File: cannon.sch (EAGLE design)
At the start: 55 parts, among them J1 RJ45

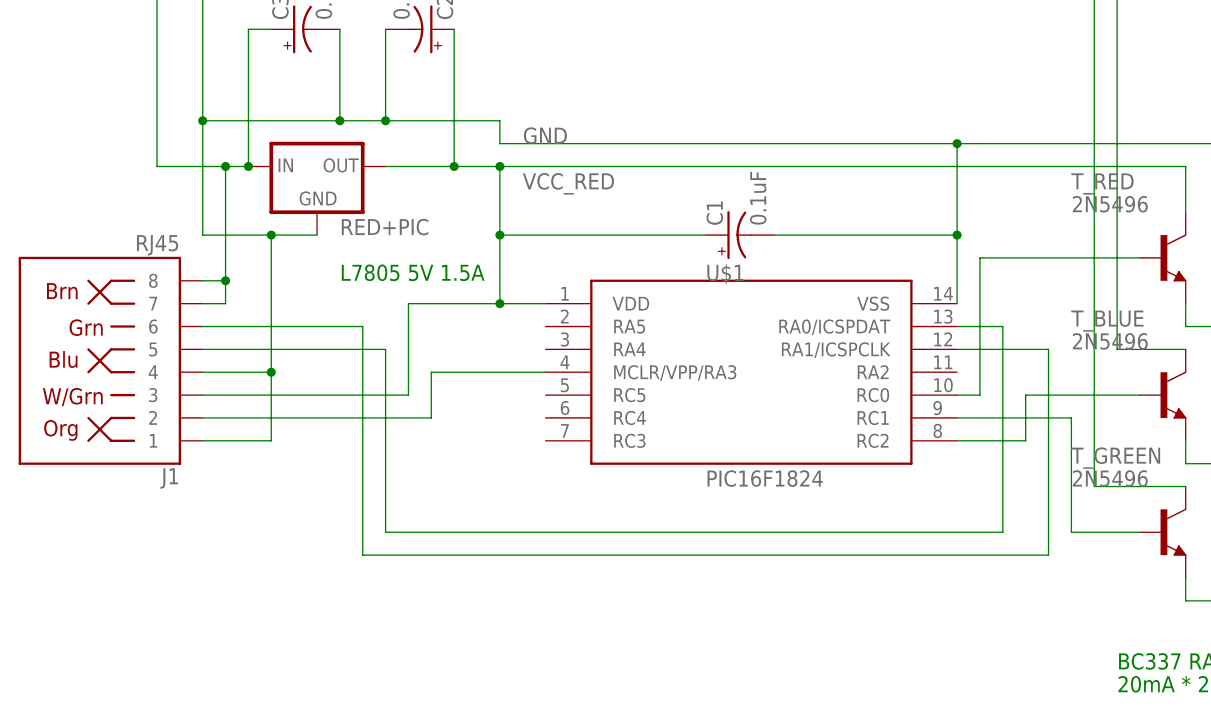
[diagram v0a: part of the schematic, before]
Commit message: Updated Board, Removed In Circuit programming
Adjusted RJ45 pins for POE standard BOARD DESIGN NOT CHANGED!!! DO NOT USE TO MAKE BOARDS
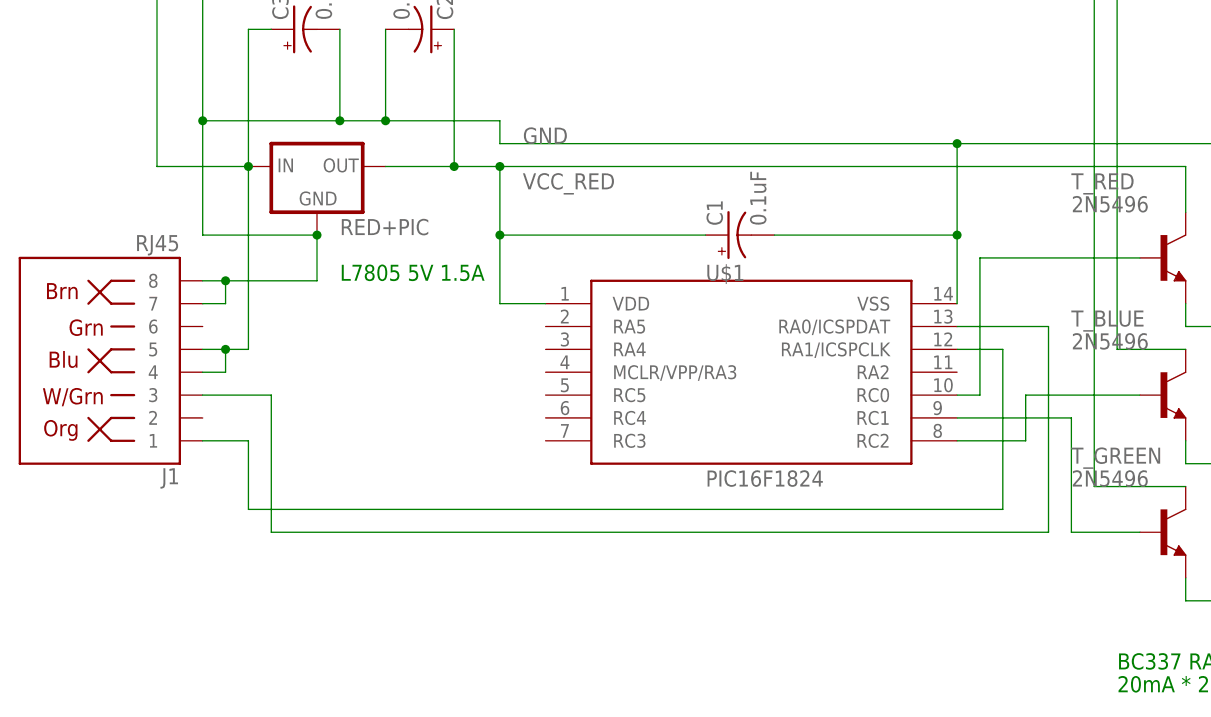
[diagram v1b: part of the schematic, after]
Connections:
- removed net N$23: J1.5, U$1.RA0/ICSPDAT
- removed net N$24: J1.6, U$1.RA1/ICSPCLK
- removed net N$8: J1.2, U$1.MCLR/VPP/RA3
- new net N$1: J1.1, U$1.RA1/ICSPCLK
- new net N$2: J1.3, U$1.RA0/ICSPDAT
- net GND: now also J1.7, J1.8; no longer J1.1, J1.4
- net N$25: now also J1.4, J1.5; no longer J1.7, J1.8
- net VCC_RED: no longer J1.3
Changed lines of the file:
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@@
 <?xml version="1.0" encoding="utf-8"?>
 <!DOCTYPE eagle SYSTEM "eagle.dtd">
-<eagle version="9.3.0">
+<eagle version="9.3.2">
 <drawing>
 <settings>
@@
 <wire x1="-12.7" y1="71.12" x2="10.16" y2="71.12" width="0.1524" layer="91"/>
 <junction x="-12.7" y="71.12"/>
-<pinref part="J1" gate="JP1" pin="3"/>
-<wire x1="-45.72" y1="53.34" x2="-22.86" y2="53.34" width="0.1524" layer="91"/>
-<wire x1="-22.86" y1="53.34" x2="-22.86" y2="63.5" width="0.1524" layer="91"/>
-<wire x1="-22.86" y1="63.5" x2="-12.7" y2="63.5" width="0.1524" layer="91"/>
-<junction x="-12.7" y="63.5"/>
 <pinref part="C2" gate="G$1" pin="+"/>
 <wire x1="-17.78" y1="93.98" x2="-17.78" y2="78.74" width="0.1524" layer="91"/>
@@
 </segment>
 </net>
-<net name="N$23" class="0">
-<segment>
-<pinref part="U$1" gate="G$1" pin="RA0/ICSPDAT"/>
-<wire x1="38.1" y1="60.96" x2="43.18" y2="60.96" width="0.1524" layer="91"/>
-<wire x1="43.18" y1="60.96" x2="43.18" y2="38.1" width="0.1524" layer="91"/>
-<pinref part="J1" gate="JP1" pin="5"/>
-<wire x1="-45.72" y1="58.42" x2="-25.4" y2="58.42" width="0.1524" layer="91"/>
-<wire x1="-25.4" y1="58.42" x2="-25.4" y2="38.1" width="0.1524" layer="91"/>
-<wire x1="-25.4" y1="38.1" x2="43.18" y2="38.1" width="0.1524" layer="91"/>
-</segment>
-</net>
-<net name="N$24" class="0">
-<segment>
-<pinref part="U$1" gate="G$1" pin="RA1/ICSPCLK"/>
-<wire x1="38.1" y1="58.42" x2="48.26" y2="58.42" width="0.1524" layer="91"/>
-<wire x1="48.26" y1="58.42" x2="48.26" y2="35.56" width="0.1524" layer="91"/>
-<pinref part="J1" gate="JP1" pin="6"/>
-<wire x1="-45.72" y1="60.96" x2="-27.94" y2="60.96" width="0.1524" layer="91"/>
-<wire x1="-27.94" y1="60.96" x2="-27.94" y2="35.56" width="0.1524" layer="91"/>
-<wire x1="-27.94" y1="35.56" x2="48.26" y2="35.56" width="0.1524" layer="91"/>
-</segment>
-</net>
-<net name="N$8" class="0">
-<segment>
-<pinref part="J1" gate="JP1" pin="2"/>
-<wire x1="-45.72" y1="50.8" x2="-20.32" y2="50.8" width="0.1524" layer="91"/>
-<wire x1="-20.32" y1="50.8" x2="-20.32" y2="55.88" width="0.1524" layer="91"/>
-<pinref part="U$1" gate="G$1" pin="MCLR/VPP/RA3"/>
-<wire x1="-20.32" y1="55.88" x2="-7.62" y2="55.88" width="0.1524" layer="91"/>
-</segment>
-</net>
 <net name="VCC_BLUE" class="0">
 <segment>
@@
 <wire x1="-40.64" y1="121.92" x2="-50.8" y2="121.92" width="0.1524" layer="91"/>
 <junction x="-40.64" y="121.92"/>
-<wire x1="-43.18" y1="78.74" x2="-40.64" y2="78.74" width="0.1524" layer="91"/>
-<pinref part="J1" gate="JP1" pin="8"/>
-<wire x1="-45.72" y1="66.04" x2="-43.18" y2="66.04" width="0.1524" layer="91"/>
-<wire x1="-43.18" y1="66.04" x2="-43.18" y2="78.74" width="0.1524" layer="91"/>
-<pinref part="J1" gate="JP1" pin="7"/>
-<wire x1="-45.72" y1="63.5" x2="-43.18" y2="63.5" width="0.1524" layer="91"/>
-<wire x1="-43.18" y1="63.5" x2="-43.18" y2="66.04" width="0.1524" layer="91"/>
-<junction x="-43.18" y="66.04"/>
 <pinref part="C3" gate="G$1" pin="+"/>
 <wire x1="-38.1" y1="93.98" x2="-40.64" y2="93.98" width="0.1524" layer="91"/>
@@
 <junction x="-40.64" y="78.74"/>
 <wire x1="-50.8" y1="121.92" x2="-50.8" y2="78.74" width="0.1524" layer="91"/>
-<wire x1="-50.8" y1="78.74" x2="-43.18" y2="78.74" width="0.1524" layer="91"/>
-<junction x="-43.18" y="78.74"/>
+<wire x1="-50.8" y1="78.74" x2="-40.64" y2="78.74" width="0.1524" layer="91"/>
 <pinref part="BLUE" gate="G$1" pin="IN"/>
 <wire x1="-40.64" y1="154.94" x2="-50.8" y2="154.94" width="0.1524" layer="91"/>
@@
 <wire x1="-40.64" y1="170.18" x2="-40.64" y2="154.94" width="0.1524" layer="91"/>
 <junction x="-40.64" y="154.94"/>
+<pinref part="J1" gate="JP1" pin="5"/>
+<wire x1="-40.64" y1="58.42" x2="-40.64" y2="78.74" width="0.1524" layer="91"/>
+<wire x1="-45.72" y1="58.42" x2="-43.18" y2="58.42" width="0.1524" layer="91"/>
+<pinref part="J1" gate="JP1" pin="4"/>
+<wire x1="-43.18" y1="58.42" x2="-40.64" y2="58.42" width="0.1524" layer="91"/>
+<wire x1="-45.72" y1="55.88" x2="-43.18" y2="55.88" width="0.1524" layer="91"/>
+<wire x1="-43.18" y1="55.88" x2="-43.18" y2="58.42" width="0.1524" layer="91"/>
+<junction x="-43.18" y="58.42"/>
 </segment>
 </net>
@@
 <wire x1="38.1" y1="81.28" x2="-12.7" y2="81.28" width="0.1524" layer="91"/>
 <junction x="38.1" y="81.28"/>
-<wire x1="-33.02" y1="71.12" x2="-38.1" y2="71.12" width="0.1524" layer="91"/>
-<wire x1="-38.1" y1="71.12" x2="-45.72" y2="71.12" width="0.1524" layer="91"/>
+<wire x1="-33.02" y1="71.12" x2="-45.72" y2="71.12" width="0.1524" layer="91"/>
 <wire x1="-45.72" y1="71.12" x2="-45.72" y2="83.82" width="0.1524" layer="91"/>
 <wire x1="-45.72" y1="83.82" x2="-30.48" y2="83.82" width="0.1524" layer="91"/>
@@
 <wire x1="17.78" y1="71.12" x2="38.1" y2="71.12" width="0.1524" layer="91"/>
 <junction x="38.1" y="71.12"/>
-<pinref part="J1" gate="JP1" pin="1"/>
-<wire x1="-45.72" y1="48.26" x2="-38.1" y2="48.26" width="0.1524" layer="91"/>
-<wire x1="-38.1" y1="48.26" x2="-38.1" y2="55.88" width="0.1524" layer="91"/>
-<junction x="-38.1" y="71.12"/>
-<pinref part="J1" gate="JP1" pin="4"/>
-<wire x1="-38.1" y1="55.88" x2="-38.1" y2="71.12" width="0.1524" layer="91"/>
-<wire x1="-45.72" y1="55.88" x2="-38.1" y2="55.88" width="0.1524" layer="91"/>
-<junction x="-38.1" y="55.88"/>
 <pinref part="C3" gate="G$1" pin="-"/>
 <wire x1="-30.48" y1="93.98" x2="-30.48" y2="83.82" width="0.1524" layer="91"/>
@@
 <junction x="254" y="66.04"/>
 <wire x1="254" y1="66.04" x2="292.1" y2="66.04" width="0.1524" layer="91"/>
+<pinref part="J1" gate="JP1" pin="8"/>
+<wire x1="-45.72" y1="66.04" x2="-43.18" y2="66.04" width="0.1524" layer="91"/>
+<wire x1="-43.18" y1="66.04" x2="-33.02" y2="66.04" width="0.1524" layer="91"/>
+<wire x1="-33.02" y1="66.04" x2="-33.02" y2="71.12" width="0.1524" layer="91"/>
+<junction x="-33.02" y="71.12"/>
+<pinref part="J1" gate="JP1" pin="7"/>
+<wire x1="-45.72" y1="63.5" x2="-43.18" y2="63.5" width="0.1524" layer="91"/>
+<wire x1="-43.18" y1="63.5" x2="-43.18" y2="66.04" width="0.1524" layer="91"/>
+<junction x="-43.18" y="66.04"/>
 </segment>
 </net>
@@
 </segment>
 </net>
+<net name="N$1" class="0">
+<segment>
+<pinref part="U$1" gate="G$1" pin="RA1/ICSPCLK"/>
+<wire x1="38.1" y1="58.42" x2="43.18" y2="58.42" width="0.1524" layer="91"/>
+<wire x1="43.18" y1="58.42" x2="43.18" y2="40.64" width="0.1524" layer="91"/>
+<wire x1="43.18" y1="40.64" x2="-40.64" y2="40.64" width="0.1524" layer="91"/>
+<wire x1="-40.64" y1="40.64" x2="-40.64" y2="48.26" width="0.1524" layer="91"/>
+<pinref part="J1" gate="JP1" pin="1"/>
+<wire x1="-40.64" y1="48.26" x2="-45.72" y2="48.26" width="0.1524" layer="91"/>
+</segment>
+</net>
+<net name="N$2" class="0">
+<segment>
+<pinref part="U$1" gate="G$1" pin="RA0/ICSPDAT"/>
+<wire x1="38.1" y1="60.96" x2="48.26" y2="60.96" width="0.1524" layer="91"/>
+<wire x1="48.26" y1="60.96" x2="48.26" y2="38.1" width="0.1524" layer="91"/>
+<wire x1="48.26" y1="38.1" x2="-38.1" y2="38.1" width="0.1524" layer="91"/>
+<pinref part="J1" gate="JP1" pin="3"/>
+<wire x1="-38.1" y1="38.1" x2="-38.1" y2="53.34" width="0.1524" layer="91"/>
+<wire x1="-38.1" y1="53.34" x2="-45.72" y2="53.34" width="0.1524" layer="91"/>
+</segment>
+</net>

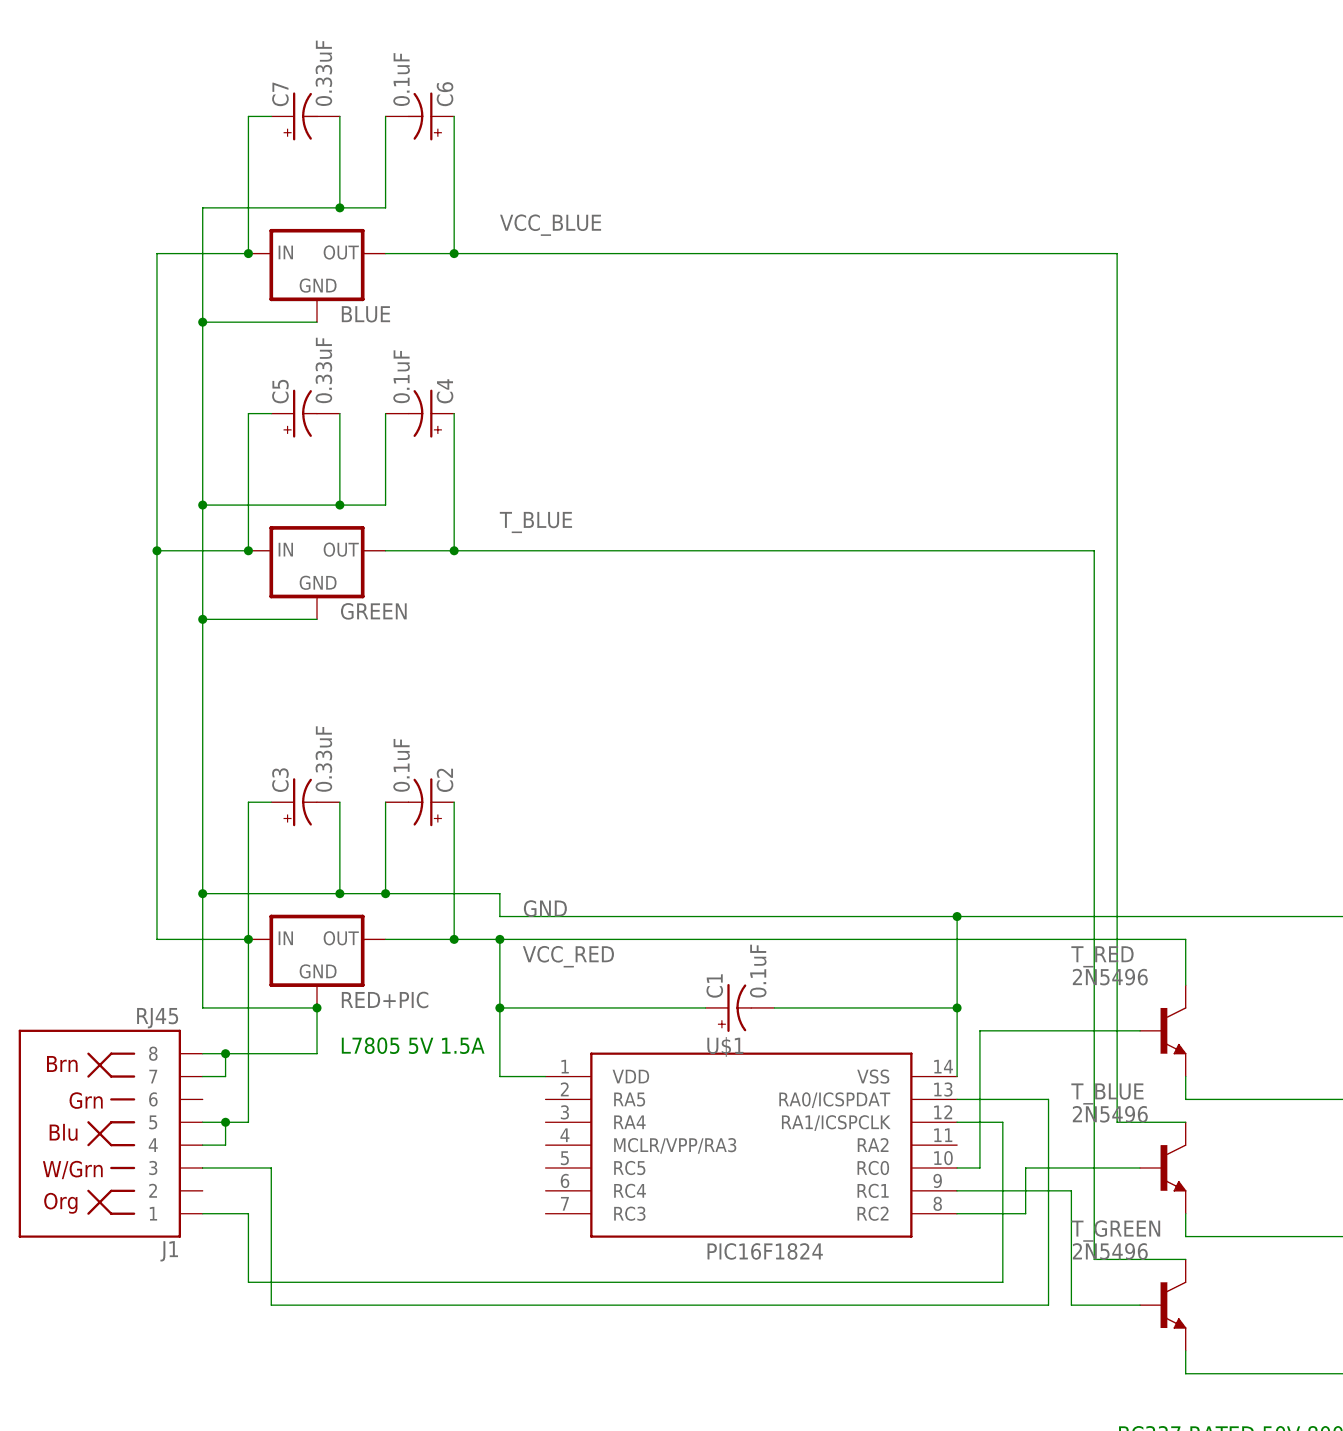
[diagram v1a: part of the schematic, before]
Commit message: Updated everything
Updated capacitor size, transistor pad, power reg pad, and LED pad
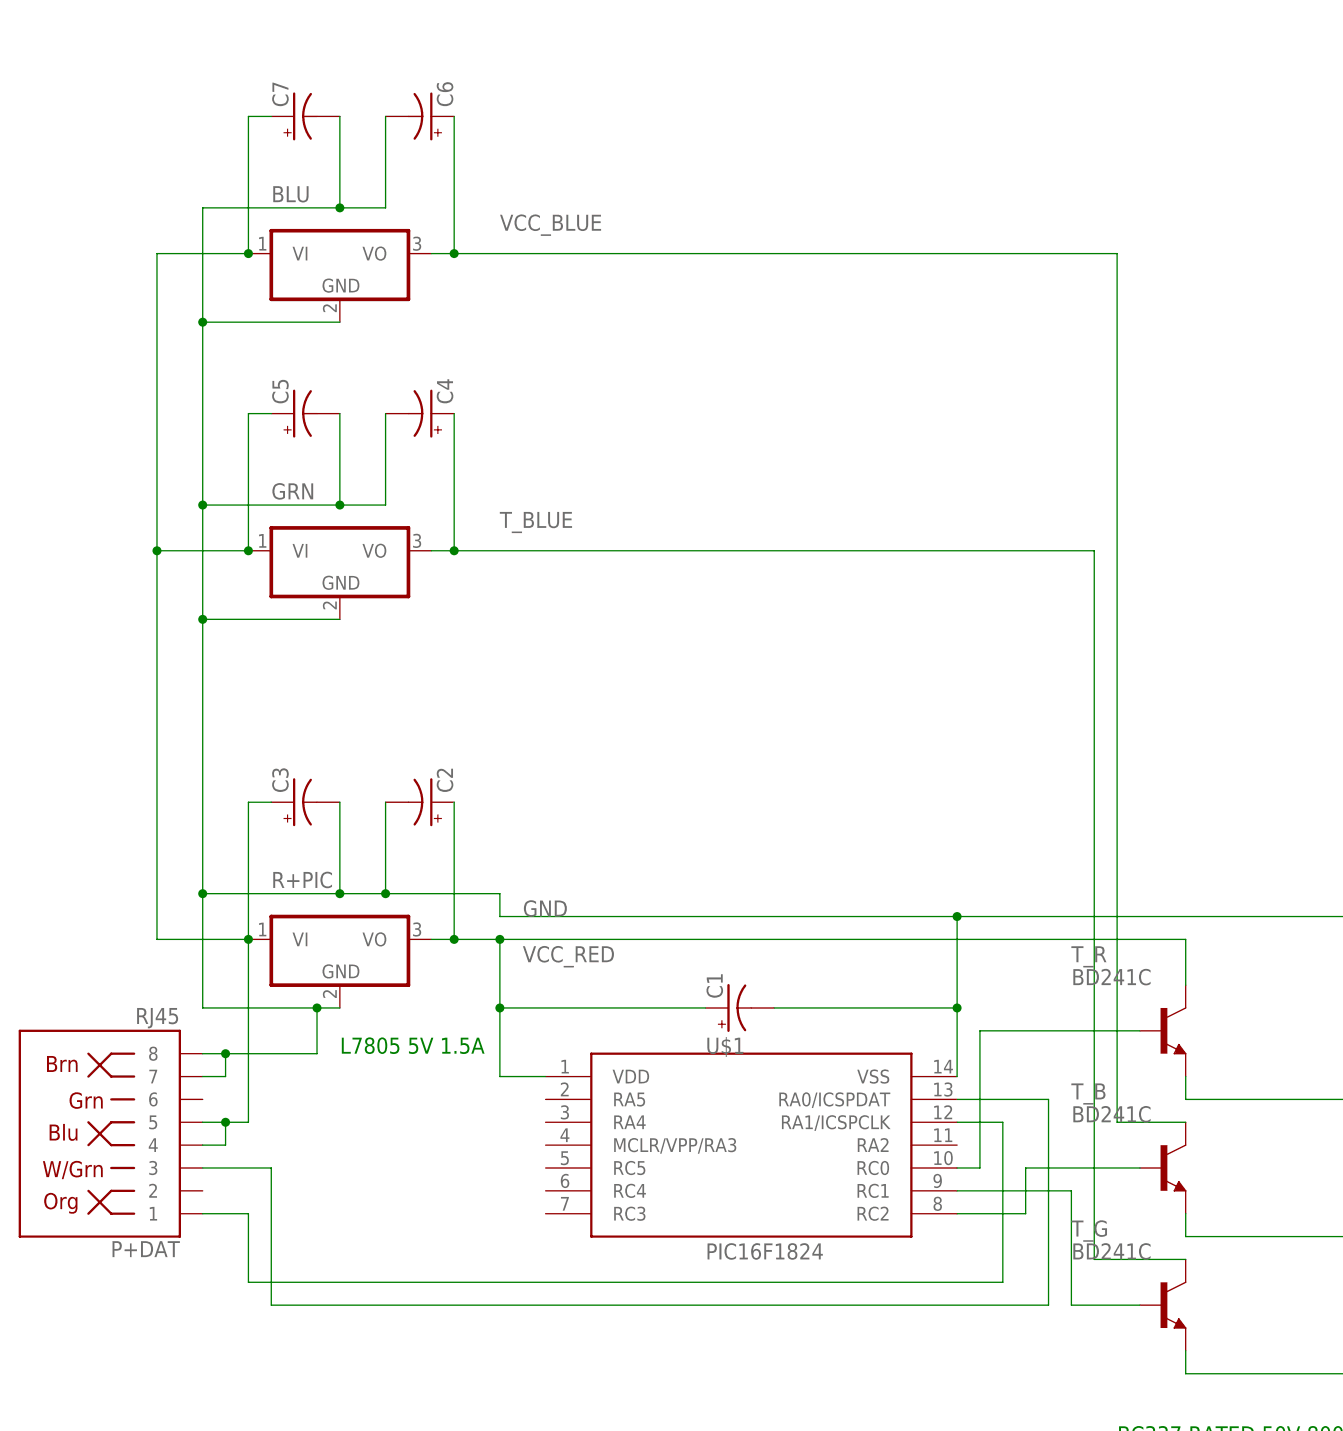
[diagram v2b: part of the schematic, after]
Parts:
- removed BLUE, GREEN, RED+PIC: (no value), SparkFun-IC-Power:V_REG_78XX-TO-220
- removed T_BLUE, T_GREEN, T_RED: 2N5496, transistor:2N5496
- added BLU, GRN, R+PIC: 7805TV, linear:7805TV
- added T_B, T_G, T_R: BD241C, transistor:2SC1306
- C1, C2, C3, C4, C5, C6, C7: device SparkFun-Capacitors:1000UF-RADIAL-5MM-25V-20% -> BeagleBone_Blue_R3:CAPACITOR-PE2.5-6
- D1, D10, D11, D12, D13, D14, D15, D16, D17, D18, D19, D2, D20, D21, D22, D23, D24, D25, D3, D4, D5, D6, D7, D8, D9: device SparkFun-LED:LED-RGB-CCCLEAR -> SparkFun-LED_MOD:LED-RGB-CCCLEAR
- renumbered J1 to P+DAT
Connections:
- net GND: now also BLU.GND, GRN.GND, R+PIC.GND; no longer BLUE.GND, GREEN.GND, RED+PIC.GND
- net N$17: now also T_B.E; no longer T_BLUE.E
- net N$22: now also T_G.E; no longer T_GREEN.E
- net N$25: now also BLU.VI, GRN.VI, R+PIC.VI; no longer BLUE.IN, GREEN.IN, RED+PIC.IN
- net N$4: now also T_R.E; no longer T_RED.E
- net N$5: now also T_R.B; no longer T_RED.B
- net N$6: now also T_G.B; no longer T_GREEN.B
- net N$7: now also T_B.B; no longer T_BLUE.B
- net T_BLUE: now also GRN.VO, T_G.C; no longer GREEN.OUT, T_GREEN.C
- net VCC_BLUE: now also BLU.VO, T_B.C; no longer BLUE.OUT, T_BLUE.C
- net VCC_RED: now also R+PIC.VO, T_R.C; no longer RED+PIC.OUT, T_RED.C
